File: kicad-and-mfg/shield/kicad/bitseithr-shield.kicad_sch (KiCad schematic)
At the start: 70 parts, among them CN1 SHIELD CONN 2, CN10 SHIELD CONN 3, CN11 SHIELD CONN 4, CN12 SHIELD CONN 5, CN2 SHIELD CONN 7, CN3 SHIELD CONN 8, CN4 PIGTAIL 4, CN5 PIGTAIL 3, CN6 PIGTAIL 5, CN7 PIGTAIL 1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

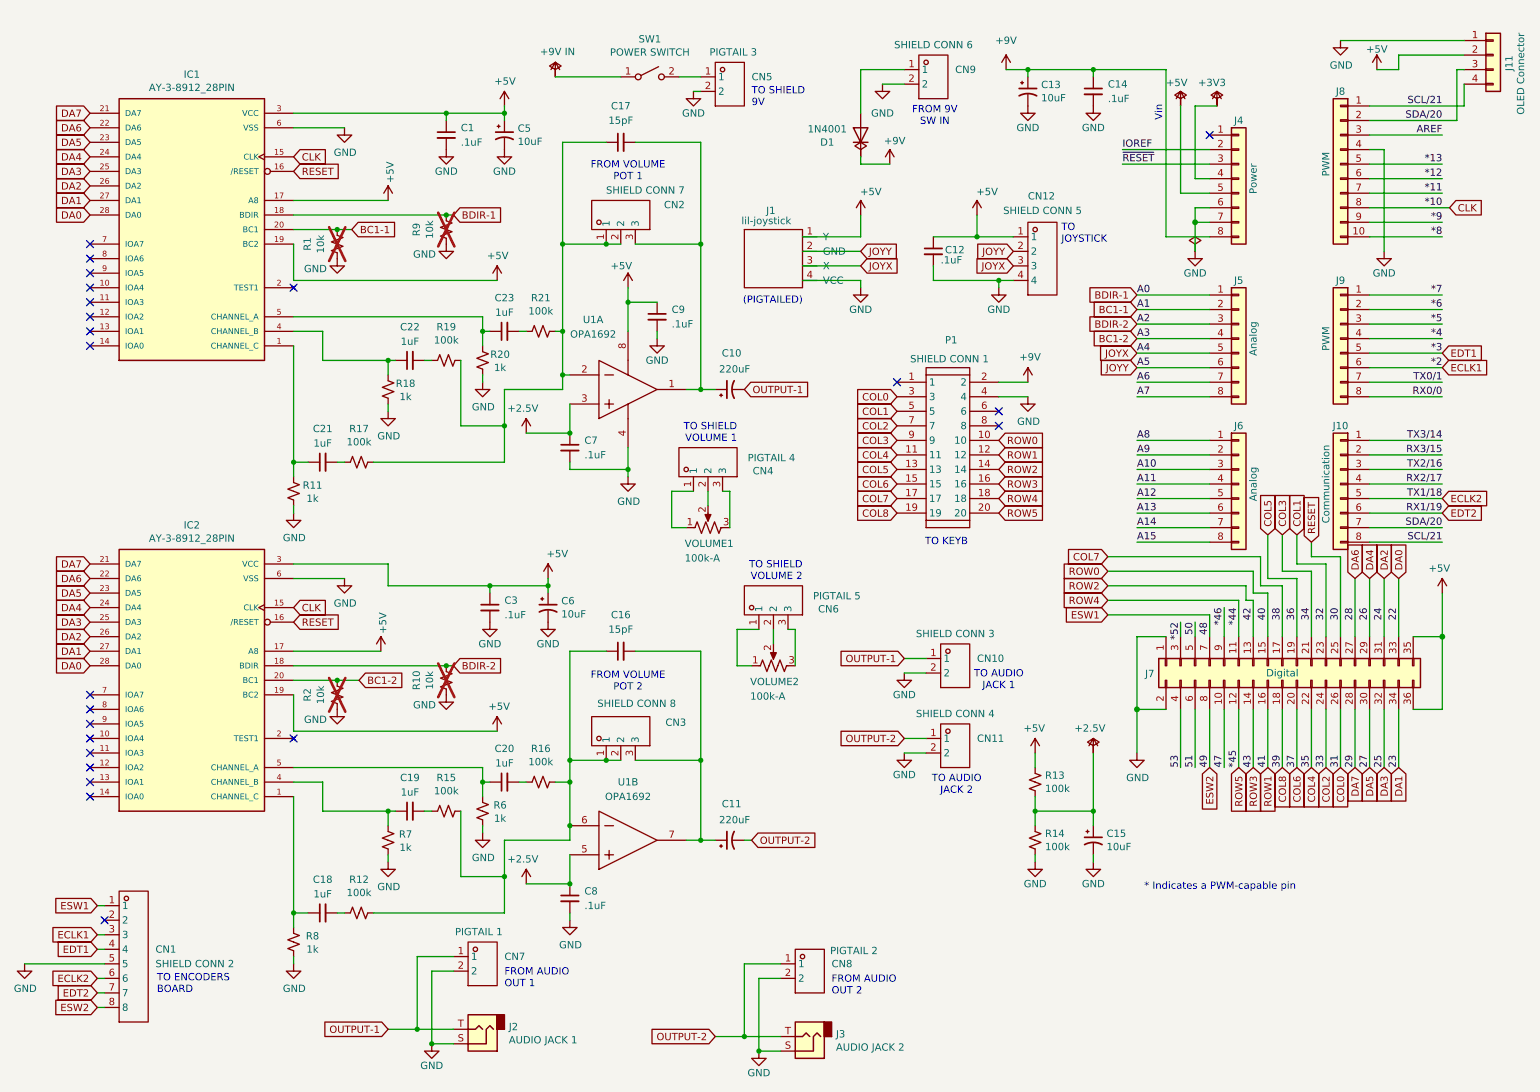
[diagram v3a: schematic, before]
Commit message: removed unneeded components from the shield schematic
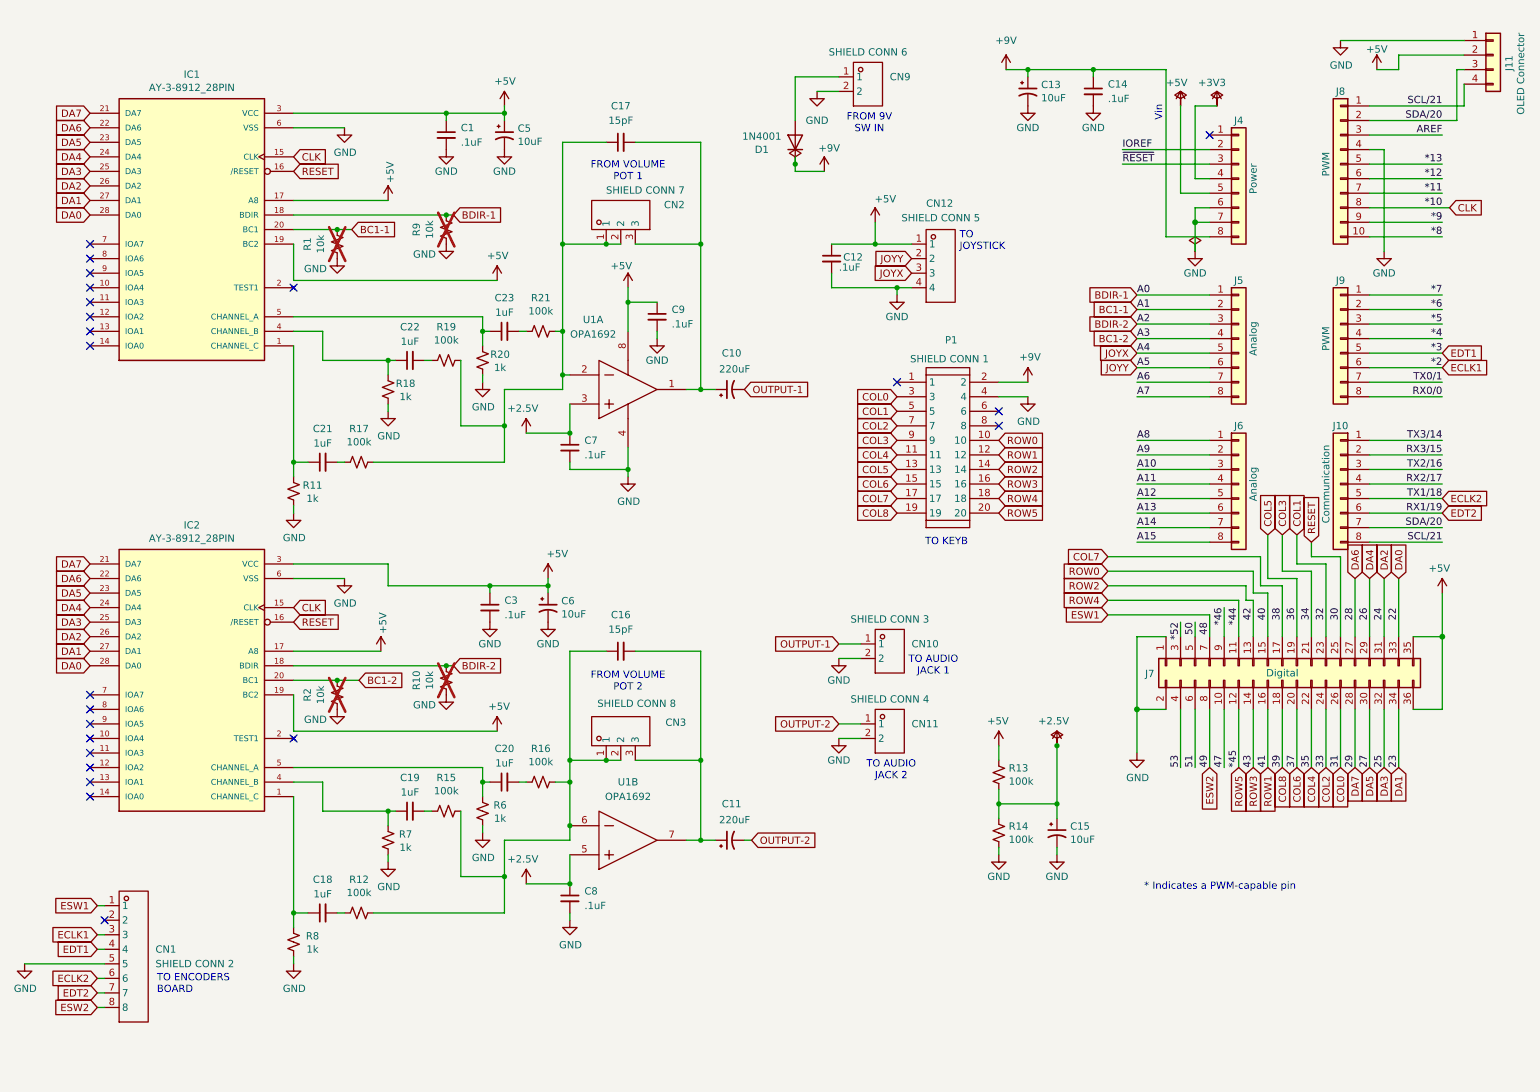
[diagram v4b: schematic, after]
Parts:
- removed CN4: PIGTAIL 4, EasyEDA_Lib:CONN-TH_3P-P2.50_HCTL_HC-XA-3AW, symbol bitseithr-shield:HC-XA-3AW
- removed CN5: PIGTAIL 3, EasyEDA_Lib:CONN-TH_2P-P2.50_HCTL_HC-XA-2AW, symbol bitseithr-shield:HC-XA-2AW
- removed CN6: PIGTAIL 5, EasyEDA_Lib:CONN-TH_3P-P2.50_HCTL_HC-XA-3AW, symbol bitseithr-shield:HC-XA-3AW
- removed CN7: PIGTAIL 1, EasyEDA_Lib:CONN-TH_2P-P2.50_HCTL_HC-XA-2AW, symbol bitseithr-shield:HC-XA-2AW
- removed CN8: PIGTAIL 2, EasyEDA_Lib:CONN-TH_2P-P2.50_HCTL_HC-XA-2AW, symbol bitseithr-shield:HC-XA-2AW
- removed J1: lil-joystick, cholm-footprints:Joystick-breakout-upside-down, symbol clholm-kicad-lib:psp-joystick
- removed J2: AUDIO JACK 1, Connector_Audio:Jack_6.35mm_Neutrik_NMJ4HCD2_Horizontal, symbol Connector_Audio:AudioJack2
- removed J3: AUDIO JACK 2, Connector_Audio:Jack_6.35mm_Neutrik_NMJ4HCD2_Horizontal, symbol Connector_Audio:AudioJack2
- removed SW1: POWER SWITCH, symbol Switch:SW_SPST
- removed VOLUME1, VOLUME2: 100k-A, clholm-kicad-library:16MM_T.MOUNT, symbol Device:R_Potentiometer_US
- C16, C17: LCSC (none) -> C106997
- C18, C19, C20, C21, C22, C23: LCSC (none) -> C92673
- R1, R10, R2, R9: footprint (none) -> Resistor_THT:R_Axial_DIN0207_L6.3mm_D2.5mm_P7.62mm_Horizontal
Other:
- note removed: "(PIGTAILED)"
- note removed: "FROM AUDIO OUT 1"
- note removed: "FROM AUDIO OUT 2"
- note removed: "TO SHIELD 9V"
- note removed: "TO SHIELD VOLUME 1"
- note removed: "TO SHIELD VOLUME 2"
- moved on the sheet: C12, C15, CN10, CN11, CN12, CN9, D1, R13, R14
